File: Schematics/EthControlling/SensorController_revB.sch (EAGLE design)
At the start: 40 parts, among them IC2 MEGA164P/324P/644P-AU, IC4 4066D, Q1 20.000M, T1 2SC1815, T3 2SC1815, T5 2SC1815, T6 2SC1815

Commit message: ditto
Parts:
- removed A_OUT1: SERIAL_SENSORXH, myparts:SERIAL_SENSORXH
- removed C9: (no value), rcl:CPOL-EUE2.5-5
- removed F4: POLYSWITCH, myparts:POLYSWITCH
- removed L2: (no value), rcl:L-US0207/10
- removed R5: 1k, rcl:R-EU_R0603
- removed R6: (no value), rcl:R-EU_0207/7
- removed T2: (no value), zetex:NMOS2SO8
- removed T3, T5, T6: 2SC1815, myparts:2SC1815
- removed U$1: TLP621-2, myparts:TLP621-2
- added B_OUT: SERIAL_SENSORXH, myparts:SERIAL_SENSORXH
- added T4: (no value), zetex:NMOSSOT23
- R1, R4: value 1k -> 100k
- R10, R3, R9: value 1k -> 10k
- R11, R12, R7, R8: value 330 -> 1k
- R2: value (none) -> 10k; device rcl:R-EU_0207/7 -> rcl:R-EU_R0603
- T1: value 2SC1815 -> (none); device myparts:2SC1815 -> zetex:NMOSSOT23
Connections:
- removed net +12V: L2.2, R2.2, R6.2, U$1G$1.3, U$1G$2.3
- removed net N$11: R5.2, U$1G$2.1
- removed net N$12: T5.B, T5.C, T6.B, U$1G$2.4
- removed net N$13: R6.1, T2B.G, T6.C
- removed net N$14: A_OUT1.CHAIN, IC4D.B, R3.1
- removed net N$15: A_OUT1.TRANS, IC4C.B, R4.1
- removed net N$16: C9.+, F1.2, L2.1
- removed net N$19: A_OUT1.VCC, F4.1, T2B.D
- removed net N$8: R2.1, T2A.G, T3.C
- net +5V: now also F1.2, R2.2; no longer F4.2, R4.2
- net A_LED: now also IC2.(ADC2/PCINT2)PA2, R1.2, T4.G; no longer IC2.(ADC1/PCINT1)PA1, R1.1
- net A_SET: now also IC2.(ADC3/PCINT3)PA3; no longer IC2.(ADC0/PCINT0)PA0
- net B_LED: now also IC2.(ADC1/PCINT1)PA1, R4.2, T1.G; no longer IC2.(ADC2/PCINT2)PA2, R5.1
- net B_SET: now also IC2.(ADC0/PCINT0)PA0; no longer IC2.(ADC3/PCINT3)PA3
- net GND: now also B_OUT.GND, R1.1, R4.1, T1.S, T4.S; no longer A_OUT1.GND, C9.-, T1.E, T3.E, T5.E, T6.E, U$1G$1.2, U$1G$2.2
- net N$1: now also T4.D; no longer T2A.S
- net N$10: now also IC4B.B; no longer IC4A.B
- net N$18: no longer T2A.D
- net N$3: now also B_OUT.CHAIN, IC4C.B, R2.1; no longer CONN1.1_12V, CONN1.2_12V, CONN1.4_12V, F1.1
- net N$5: now also B_OUT.TRANS, IC4D.B, R3.1; no longer R1.2, U$1G$1.1
- net N$6: now also B_OUT.VCC, F1.1; no longer T1.B, T1.C, T3.B, U$1G$1.4
- net N$7: now also B_OUT.VLED, T1.D; no longer A_OUT1.VLED, T2B.S
- net N$9: now also IC4A.B; no longer IC4B.B
- net RX0: now also IC4B.A, IC4D.A; no longer IC4A.A, IC4C.A
- net TX0: now also IC4A.A, IC4C.A; no longer IC4B.A, IC4D.A
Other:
- moved on the sheet: F1, F2, IC4A, IC4B, IC4C, IC4D, R1, R2, R3, R4

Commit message: ditto
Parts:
- added A_OUT1, A_OUT2, A_OUT3, B_OUT1, B_OUT2, B_OUT3: SERIAL_SENSORXH, myparts:SERIAL_SENSORXH
- added C4, C5, C9: 0.1u, rcl:C-EUC1608
- added F4, F5, F6, F7, F8, F9: POLYSWITCH, myparts:POLYSWITCH
- added IC1, IC3, IC5: 4066D, 40xx:4066D
- added R13, R16, R19, R22, R25, R28: 100k, rcl:R-EU_R0603
- added R14, R15, R17, R18, R20, R21, R23, R24, R26, R27, R5, R6: 10k, rcl:R-EU_R0603
- added T2, T3, T5, T6, T7, T8: (no value), zetex:NMOSSOT23
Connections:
- new net N$11: A_OUT1.TRANS, IC1B.B, R6.1
- new net N$12: A_OUT1.VCC, F4.1
- new net N$13: A_OUT1.VLED, T2.D
- new net N$14: B_OUT1.CHAIN, IC1C.B, R14.1
- new net N$15: B_OUT1.TRANS, IC1D.B, R15.1
- new net N$16: B_OUT1.VCC, F5.1
- new net N$19: B_OUT1.VLED, T3.D
- new net N$24: A_OUT2.CHAIN, IC3A.B, R17.1
- new net N$25: A_OUT2.TRANS, IC3B.B, R18.1
- new net N$26: A_OUT2.VCC, F6.1
- new net N$27: A_OUT2.VLED, T5.D
- new net N$28: B_OUT2.CHAIN, IC3C.B, R20.1
- new net N$29: B_OUT2.TRANS, IC3D.B, R21.1
- new net N$30: B_OUT2.VCC, F7.1
- new net N$31: B_OUT2.VLED, T6.D
- new net N$32: A_OUT3.CHAIN, IC5A.B, R23.1
- new net N$33: A_OUT3.TRANS, IC5B.B, R24.1
- new net N$34: A_OUT3.VCC, F8.1
- new net N$35: A_OUT3.VLED, T7.D
- new net N$36: B_OUT3.CHAIN, IC5C.B, R26.1
- new net N$37: B_OUT3.TRANS, IC5D.B, R27.1
- new net N$38: B_OUT3.VCC, F9.1
- new net N$39: B_OUT3.VLED, T8.D
- new net N$8: A_OUT1.CHAIN, IC1A.B, R5.1
- net +5V: now also C4.2, C5.2, C9.2, F4.2, F5.2, F6.2, F7.2, F8.2, F9.2, IC1P.VDD, IC3P.VDD, IC5P.VDD, R14.2, R15.2, R17.2, R18.2, R20.2, R21.2, R23.2, R24.2, R26.2, R27.2, R5.2, R6.2
- net A_LED: now also R13.2, R19.2, R25.2, T2.G, T5.G, T7.G
- net A_SET: now also IC1A.C, IC1B.C, IC3A.C, IC3B.C, IC5A.C, IC5B.C
- net B_LED: now also R16.2, R22.2, R28.2, T3.G, T6.G, T8.G
- net B_SET: now also IC1C.C, IC1D.C, IC3C.C, IC3D.C, IC5C.C, IC5D.C
- net GND: now also A_OUT1.GND, A_OUT2.GND, A_OUT3.GND, B_OUT1.GND, B_OUT2.GND, B_OUT3.GND, C4.1, C5.1, C9.1, IC1P.VSS, IC3P.VSS, IC5P.VSS, R13.1, R16.1, R19.1, R22.1, R25.1, R28.1, T2.S, T3.S, T5.S, T6.S, T7.S, T8.S
- net RX0: now also IC1B.A, IC1D.A, IC3B.A, IC3D.A, IC5B.A, IC5D.A
- net TX0: now also IC1A.A, IC1C.A, IC3A.A, IC3C.A, IC5A.A, IC5C.A
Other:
- moved on the sheet: C10, F1, F2, IC4A, IC4B, IC4C, IC4D, IC4P, R1, R10, R2, R3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

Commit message: ditto
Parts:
- renumbered A_OUT1 to C_OUT, A_OUT2 to E_OUT, A_OUT3 to G_OUT, B_OUT1 to D_OUT, B_OUT2 to F_OUT, B_OUT3 to H_OUT
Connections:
- removed net TRANS_STANDBY: IC2.(XCK1/OC1B/PCINT28)PD4
- net A_LED: no longer R13.2, R19.2, R25.2, T2.G, T5.G, T7.G
- net A_SET: now also IC2.(ADC1/PCINT1)PA1; no longer IC1A.C, IC1B.C, IC2.(ADC3/PCINT3)PA3, IC3A.C, IC3B.C, IC5A.C, IC5B.C
- net B_LED: now also IC2.(ADC3/PCINT3)PA3; no longer IC2.(ADC1/PCINT1)PA1, R16.2, R22.2, R28.2, T3.G, T6.G, T8.G
- net B_SET: no longer IC1C.C, IC1D.C, IC3C.C, IC3D.C, IC5C.C, IC5D.C
- net C_LED: now also R13.2, T2.G
- net C_SET: now also IC1A.C, IC1B.C
- net D_LED: now also R16.2, T3.G
- net D_SET: now also IC1C.C, IC1D.C
- net E_LED: now also R19.2, T5.G
- net E_SET: now also IC3A.C, IC3B.C
- net F_LED: now also R22.2, T6.G
- net F_SET: now also IC3C.C, IC3D.C
- net G_LED: now also IC2.(XCK1/OC1B/PCINT28)PD4, R25.2, T7.G; no longer IC2.(SDA/PCINT17)PC1
- net G_SET: now also IC2.(OC2A/PCINT31)PD7, IC5A.C, IC5B.C; no longer IC2.(SCL/PCINT16)PC0
- net H_LED: now also IC2.(OC1A/PCINT29)PD5, R28.2, T8.G; no longer IC2.(TOSC1/PCINT22)PC6
- net H_SET: now also IC2.(OC2B/ICP/PCINT30)PD6, IC5C.C, IC5D.C; no longer IC2.(TOSC2/PCINT23)PC7
- net RX0: no longer IC3B.A, IC3D.A, IC5B.A, IC5D.A
- net RX1: now also IC3B.A, IC3D.A, IC5B.A, IC5D.A
- net TX0: no longer IC3A.A, IC3C.A, IC5A.A, IC5C.A
- net TX1: now also IC3A.A, IC3C.A, IC5A.A, IC5C.A

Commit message: ditto
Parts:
- C3: value (none) -> 100u
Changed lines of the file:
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@@
 <part name="IC4" library="40xx" deviceset="4066" device="D"/>
 <part name="F2" library="myparts" deviceset="POLYSWITCH" device=""/>
-<part name="C3" library="rcl" deviceset="CPOL-EU" device="E2.5-5"/>
+<part name="C3" library="rcl" deviceset="CPOL-EU" device="E2.5-5" value="100u"/>
 <part name="GND14" library="supply1" deviceset="GND" device=""/>
 <part name="P+1" library="supply1" deviceset="+5V" device=""/>

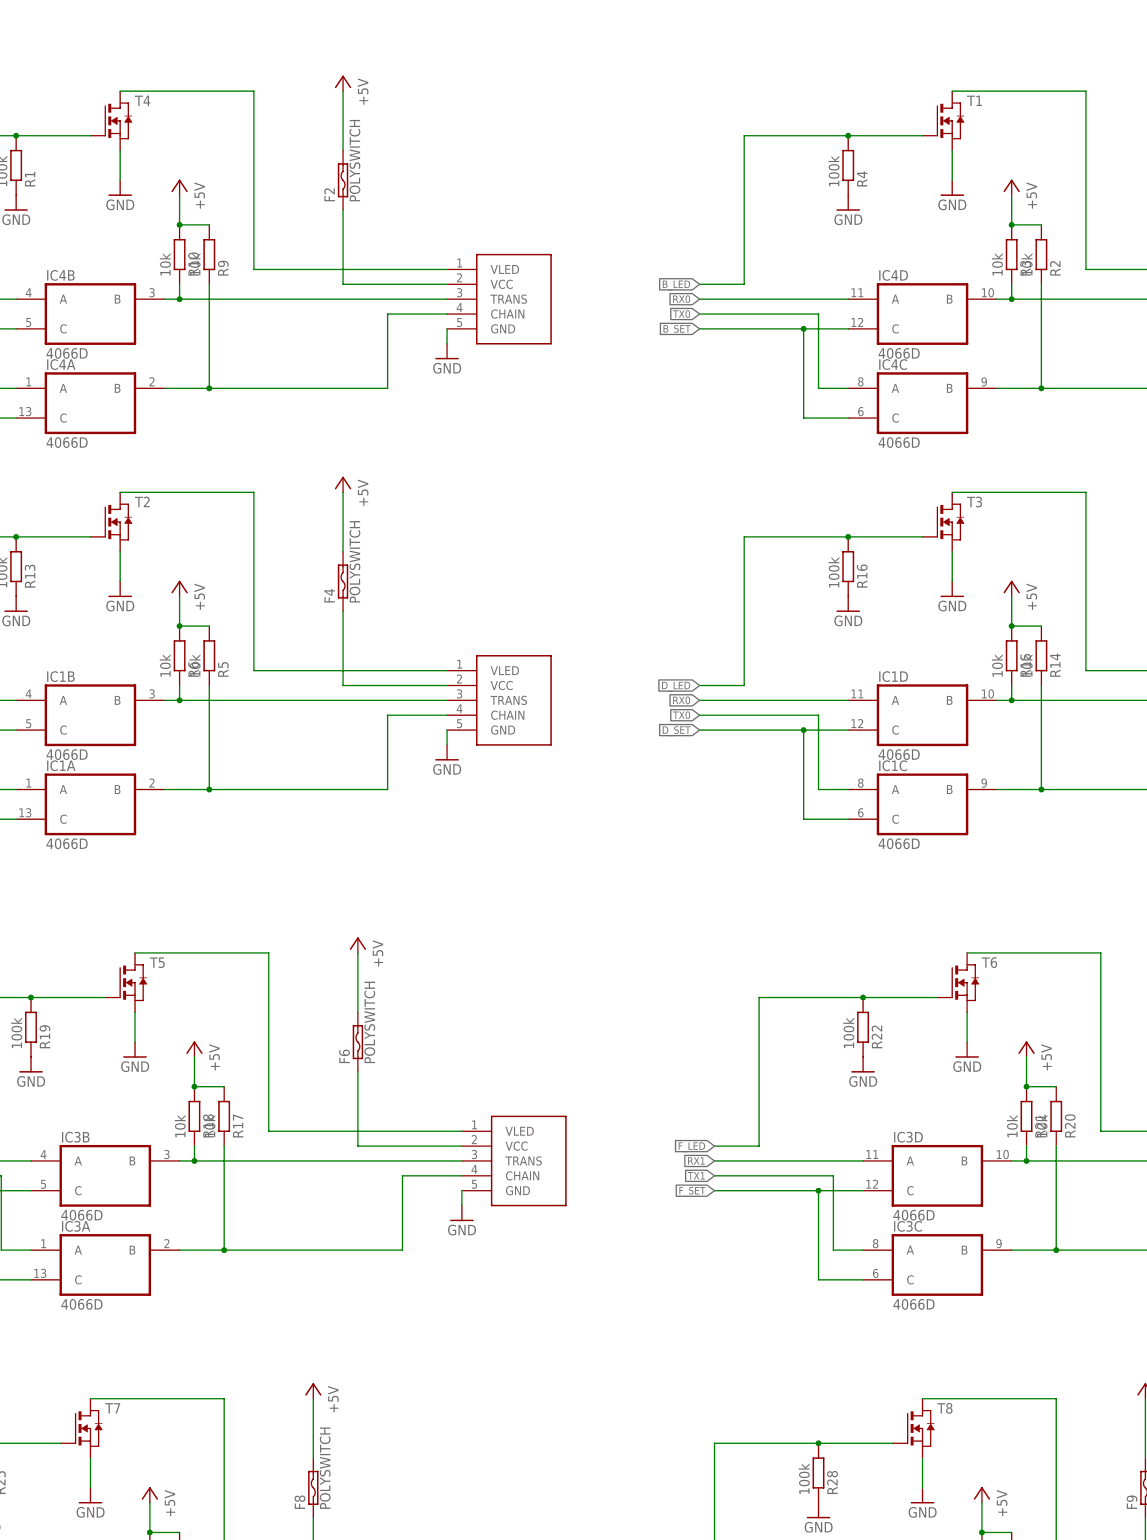
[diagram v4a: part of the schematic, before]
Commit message: associate of parts of SensorController_revB
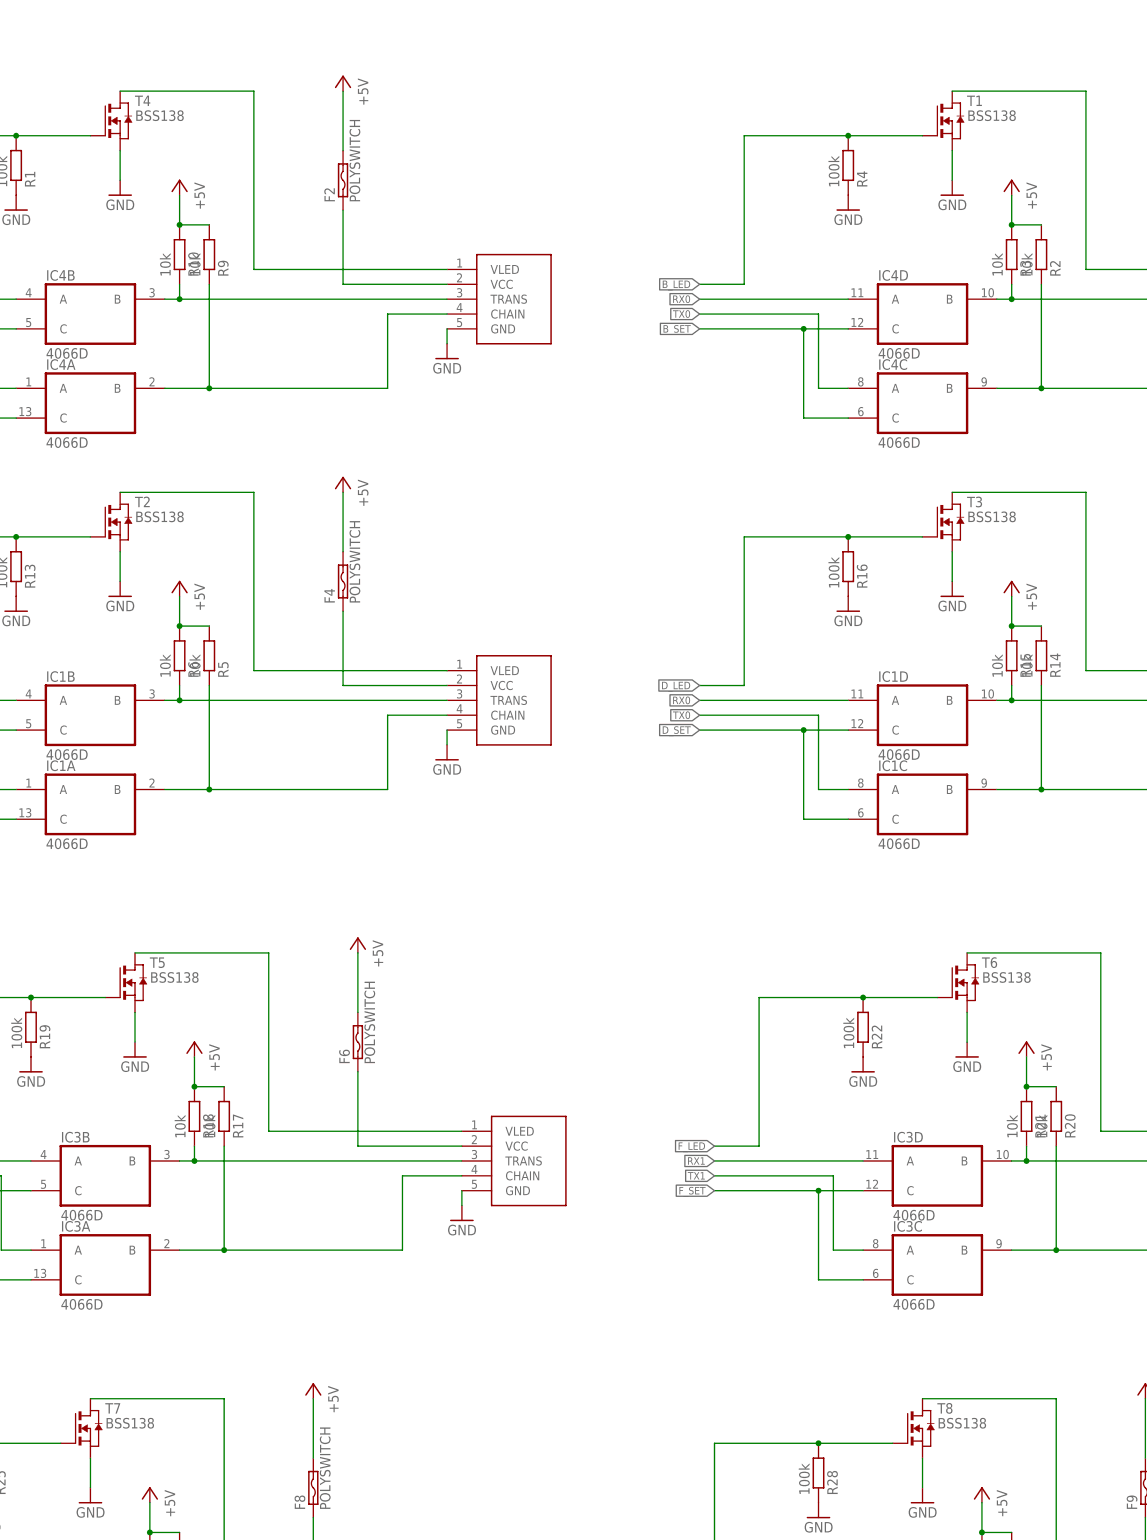
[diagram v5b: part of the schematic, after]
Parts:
- T1, T2, T3, T4, T5, T6, T7, T8: value (none) -> BSS138
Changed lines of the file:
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@@
 <part name="R11" library="rcl" deviceset="R-EU_" device="R0603" value="1k"/>
 <part name="R12" library="rcl" deviceset="R-EU_" device="R0603" value="1k"/>
-<part name="T4" library="zetex" deviceset="NMOSSOT23" device=""/>
+<part name="T4" library="zetex" deviceset="NMOSSOT23" device="" value="BSS138"/>
 <part name="GND5" library="supply1" deviceset="GND" device=""/>
 <part name="R1" library="rcl" deviceset="R-EU_" device="R0603" value="100k"/>
@@
 <part name="P+6" library="supply1" deviceset="+5V" device=""/>
 <part name="F1" library="myparts" deviceset="POLYSWITCH" device=""/>
-<part name="T1" library="zetex" deviceset="NMOSSOT23" device=""/>
+<part name="T1" library="zetex" deviceset="NMOSSOT23" device="" value="BSS138"/>
 <part name="GND9" library="supply1" deviceset="GND" device=""/>
 <part name="R4" library="rcl" deviceset="R-EU_" device="R0603" value="100k"/>
@@
 <part name="P+9" library="supply1" deviceset="+5V" device=""/>
 <part name="C4" library="rcl" deviceset="C-EU" device="C1608" value="0.1u"/>
-<part name="T2" library="zetex" deviceset="NMOSSOT23" device=""/>
+<part name="T2" library="zetex" deviceset="NMOSSOT23" device="" value="BSS138"/>
 <part name="GND13" library="supply1" deviceset="GND" device=""/>
 <part name="R13" library="rcl" deviceset="R-EU_" device="R0603" value="100k"/>
@@
 <part name="P+11" library="supply1" deviceset="+5V" device=""/>
 <part name="F5" library="myparts" deviceset="POLYSWITCH" device=""/>
-<part name="T3" library="zetex" deviceset="NMOSSOT23" device=""/>
+<part name="T3" library="zetex" deviceset="NMOSSOT23" device="" value="BSS138"/>
 <part name="GND18" library="supply1" deviceset="GND" device=""/>
 <part name="R16" library="rcl" deviceset="R-EU_" device="R0603" value="100k"/>
@@
 <part name="P+14" library="supply1" deviceset="+5V" device=""/>
 <part name="C5" library="rcl" deviceset="C-EU" device="C1608" value="0.1u"/>
-<part name="T5" library="zetex" deviceset="NMOSSOT23" device=""/>
+<part name="T5" library="zetex" deviceset="NMOSSOT23" device="" value="BSS138"/>
 <part name="GND22" library="supply1" deviceset="GND" device=""/>
 <part name="R19" library="rcl" deviceset="R-EU_" device="R0603" value="100k"/>
@@
 <part name="P+16" library="supply1" deviceset="+5V" device=""/>
 <part name="F7" library="myparts" deviceset="POLYSWITCH" device=""/>
-<part name="T6" library="zetex" deviceset="NMOSSOT23" device=""/>
+<part name="T6" library="zetex" deviceset="NMOSSOT23" device="" value="BSS138"/>
 <part name="GND25" library="supply1" deviceset="GND" device=""/>
 <part name="R22" library="rcl" deviceset="R-EU_" device="R0603" value="100k"/>
@@
 <part name="P+19" library="supply1" deviceset="+5V" device=""/>
 <part name="C9" library="rcl" deviceset="C-EU" device="C1608" value="0.1u"/>
-<part name="T7" library="zetex" deviceset="NMOSSOT23" device=""/>
+<part name="T7" library="zetex" deviceset="NMOSSOT23" device="" value="BSS138"/>
 <part name="GND29" library="supply1" deviceset="GND" device=""/>
 <part name="R25" library="rcl" deviceset="R-EU_" device="R0603" value="100k"/>
@@
 <part name="P+21" library="supply1" deviceset="+5V" device=""/>
 <part name="F9" library="myparts" deviceset="POLYSWITCH" device=""/>
-<part name="T8" library="zetex" deviceset="NMOSSOT23" device=""/>
+<part name="T8" library="zetex" deviceset="NMOSSOT23" device="" value="BSS138"/>
 <part name="GND32" library="supply1" deviceset="GND" device=""/>
 <part name="R28" library="rcl" deviceset="R-EU_" device="R0603" value="100k"/>
